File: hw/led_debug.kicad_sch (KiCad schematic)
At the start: 8 parts

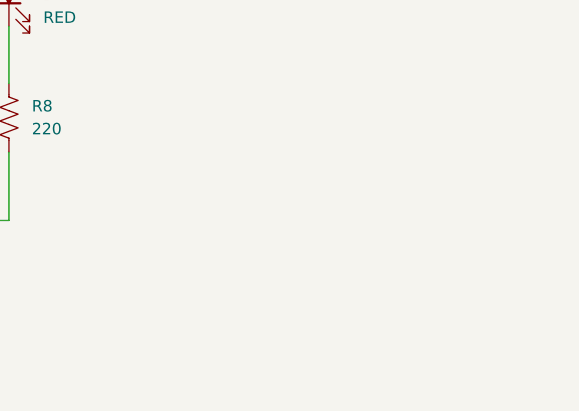
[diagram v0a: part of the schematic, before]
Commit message: Add debug pads for power rails
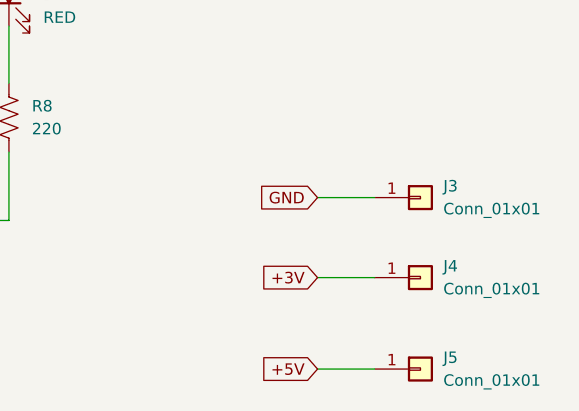
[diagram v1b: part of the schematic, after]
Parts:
- added J3, J4, J5: Conn_01x01, TestPoint:TestPoint_THTPad_1.0x1.0mm_Drill0.5mm, symbol Connector_Generic:Conn_01x01
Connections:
- net GND: now also J3.1 (Pin_1)
- new net +3V: J4.1 (Pin_1)
- new net +5V: J5.1 (Pin_1)
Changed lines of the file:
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@@
+    (stroke (width 0) (type default))
+  )
+  (wire (pts (xy 156.21 102.87) (xy 162.56 102.87))
     (stroke (width 0) (type default))
   )
@@
     (stroke (width 0) (type default))
   )
+  (wire (pts (xy 156.21 113.03) (xy 162.56 113.03))
+    (stroke (width 0) (type default))
+  )
   (wire (pts (xy 64.77 88.9) (xy 64.77 96.52))
     (stroke (width 0) (type default))
@@
   )
   (wire (pts (xy 85.09 74.93) (xy 85.09 81.28))
+    (stroke (width 0) (type default))
+  )
+  (wire (pts (xy 156.21 93.98) (xy 162.56 93.98))
     (stroke (width 0) (type default))
   )
@@
     )
   )
+  (global_label "GND" (shape input) (at 156.21 93.98 180) (fields_autoplaced)
+    (effects (font (size 1.27 1.27)) (justify right))
+    (property "Intersheetrefs" "${INTERSHEET_REFS}" (at 150.0085 93.98 0)
+      (effects (font (size 1.27 1.27)) (justify right) hide)
+    )
+  )
+  (global_label "+3V" (shape input) (at 156.21 102.87 180) (fields_autoplaced)
+    (effects (font (size 1.27 1.27)) (justify right))
+    (property "Intersheetrefs" "${INTERSHEET_REFS}" (at 150.0085 102.87 0)
+      (effects (font (size 1.27 1.27)) (justify right) hide)
+    )
+  )
+  (global_label "+5V" (shape input) (at 156.21 113.03 180) (fields_autoplaced)
+    (effects (font (size 1.27 1.27)) (justify right))
+    (property "Intersheetrefs" "${INTERSHEET_REFS}" (at 150.0085 113.03 0)
+      (effects (font (size 1.27 1.27)) (justify right) hide)
+    )
+  )
   (hierarchical_label "LED_CAN_TX" (shape input) (at 64.77 59.69 90) (fields_autoplaced)
     (effects (font (size 1.27 1.27)) (justify left))
@@
     )
   )
+  (symbol (lib_id "Connector_Generic:Conn_01x01") (at 167.64 102.87 0) (unit 1)
+    (in_bom no) (on_board yes) (dnp no) (fields_autoplaced)
+    (property "Reference" "J4" (at 170.18 101.6 0)
+      (effects (font (size 1.27 1.27)) (justify left))
+    )
+    (property "Value" "Conn_01x01" (at 170.18 104.14 0)
+      (effects (font (size 1.27 1.27)) (justify left))
+    )
+    (property "Footprint" "TestPoint:TestPoint_THTPad_1.0x1.0mm_Drill0.5mm" (at 167.64 102.87 0)
+      (effects (font (size 1.27 1.27)) hide)
+    )
+    (property "Datasheet" "~" (at 167.64 102.87 0)
+      (effects (font (size 1.27 1.27)) hide)
+    )
+    (pin "1")
+    (instances
+      (project "fdcanusb"
+        (path "/ea2f11d1-8f9e-424e-8d4d-b56c0d6c1766/729b5f27-c6cd-40a1-9ca1-bf5632e46b52"
+          (reference "J4") (unit 1)
+        )
+      )
+    )
+  )
+  (symbol (lib_id "Connector_Generic:Conn_01x01") (at 167.64 93.98 0) (unit 1)
+    (in_bom no) (on_board yes) (dnp no) (fields_autoplaced)
+    (property "Reference" "J3" (at 170.18 92.71 0)
+      (effects (font (size 1.27 1.27)) (justify left))
+    )
+    (property "Value" "Conn_01x01" (at 170.18 95.25 0)
+      (effects (font (size 1.27 1.27)) (justify left))
+    )
+    (property "Footprint" "TestPoint:TestPoint_THTPad_1.0x1.0mm_Drill0.5mm" (at 167.64 93.98 0)
+      (effects (font (size 1.27 1.27)) hide)
+    )
+    (property "Datasheet" "~" (at 167.64 93.98 0)
+      (effects (font (size 1.27 1.27)) hide)
+    )
+    (pin "1")
+    (instances
+      (project "fdcanusb"
+        (path "/ea2f11d1-8f9e-424e-8d4d-b56c0d6c1766/729b5f27-c6cd-40a1-9ca1-bf5632e46b52"
+          (reference "J3") (unit 1)
+        )
+      )
+    )
+  )
   (symbol (lib_id "Device:LED") (at 85.09 71.12 90) (unit 1)
     (in_bom yes) (on_board yes) (dnp no) (fields_autoplaced)
@@
         )
       )
+    )
+  )
+  (symbol (lib_id "Connector_Generic:Conn_01x01") (at 167.64 113.03 0) (unit 1)
+    (in_bom no) (on_board yes) (dnp no) (fields_autoplaced)
+    (property "Reference" "J5" (at 170.18 111.76 0)
+      (effects (font (size 1.27 1.27)) (justify left))
+    )
+    (property "Value" "Conn_01x01" (at 170.18 114.3 0)
+      (effects (font (size 1.27 1.27)) (justify left))
+    )
+    (property "Footprint" "TestPoint:TestPoint_THTPad_1.0x1.0mm_Drill0.5mm" (at 167.64 113.03 0)
+      (effects (font (size 1.27 1.27)) hide)
+    )
+    (property "Datasheet" "~" (at 167.64 113.03 0)
+      (effects (font (size 1.27 1.27)) hide)
+    )
+    (pin "1")
+    (instances
+      (project "fdcanusb"
+        (path "/ea2f11d1-8f9e-424e-8d4d-b56c0d6c1766/729b5f27-c6cd-40a1-9ca1-bf5632e46b52"
+          (reference "J5") (unit 1)
+        )
+      )

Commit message: Add title block and update rev to r4.2
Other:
- company: (none) -> mjbots Robotic Systems, LLC - info@mjbots.com - 2024
- title: (none) -> mjcanfd-usb-1x r4.2
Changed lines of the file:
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@@
 (kicad_sch (version 20230121) (generator eeschema)
   (paper "A4")
+  (title_block
+    (title "mjcanfd-usb-1x r4.2")
+    (company "mjbots Robotic Systems, LLC - info@mjbots.com - 2024")
+    (comment 1 "Licensed under the Apache 2.0 License")
+  )
   (junction (at 104.14 96.52) (diameter 0) (color 0 0 0 0)
   )
